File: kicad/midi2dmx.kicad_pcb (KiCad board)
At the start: 4 copper layers, 73.7 x 43.2 mm, 29 parts, among them IC1 MAX485E, P1 MIDI Input, P2 MIDI Through, P3 DMX Out, P4 9V Power, SW1 SW_LED_blue, U1 ProMini

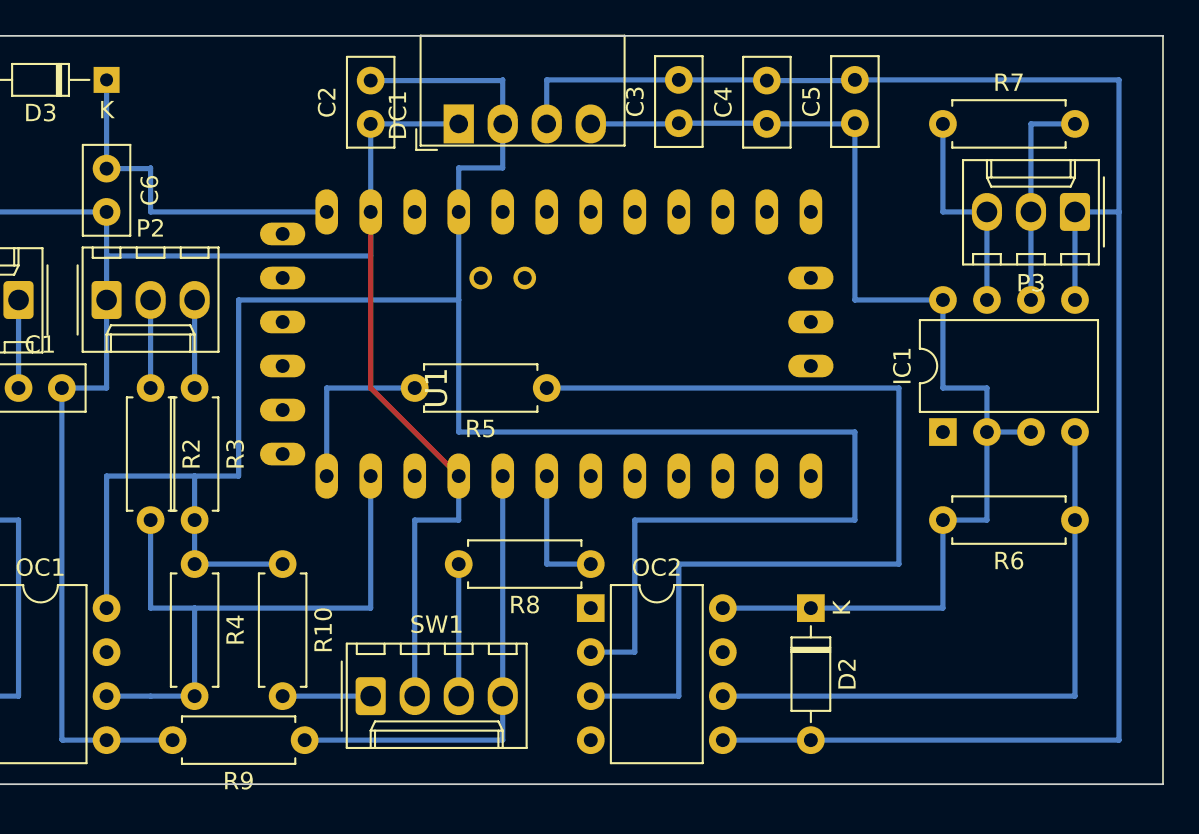
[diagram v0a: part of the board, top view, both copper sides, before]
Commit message: update schematic
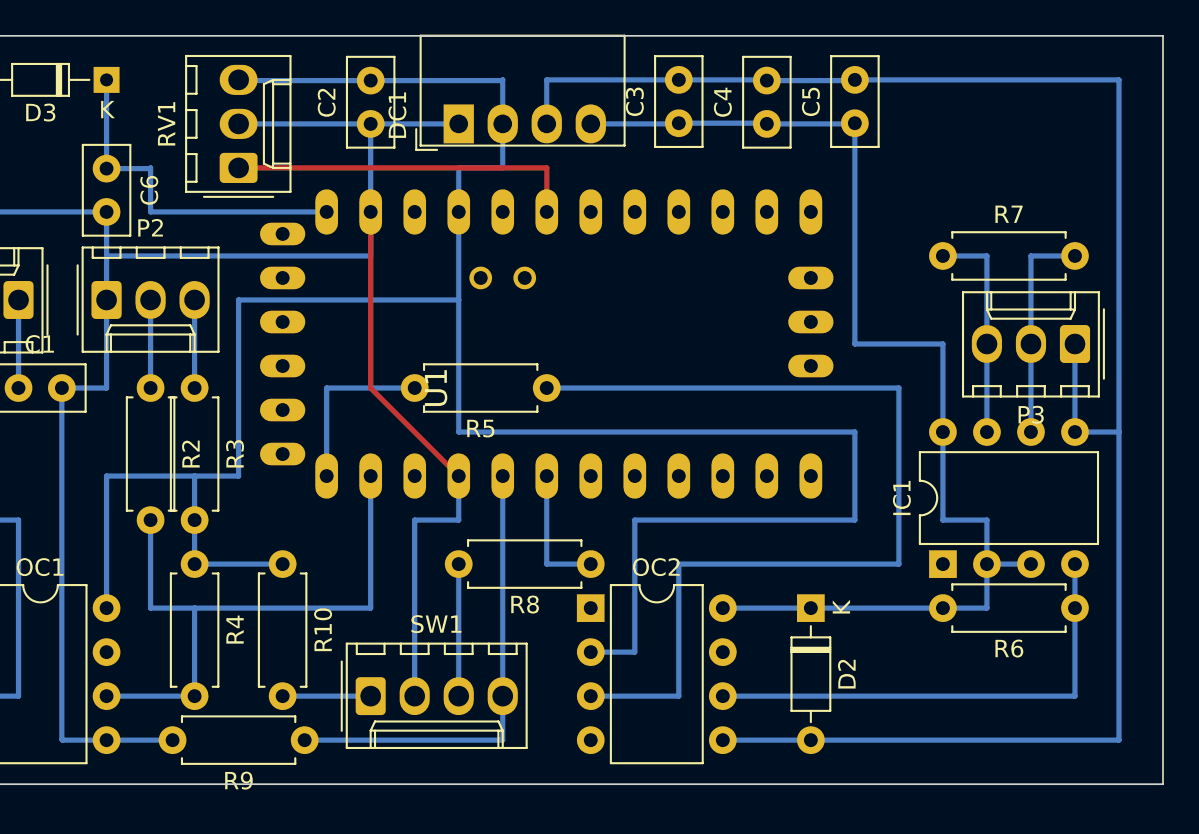
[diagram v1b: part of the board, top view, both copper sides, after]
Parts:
- added RV1: 10k, Connector_Molex:Molex_KK-254_AE-6410-03A_1x03_P2.54mm_Vertical, F.Cu at (83.8, 124.5)
- moved IC1 7.62 mm to (124.5, 147.3)
- moved P3 7.62 mm to (132.1, 134.6)
- moved R7 7.62 mm to (124.5, 129.5)
- moved R6 5.08 mm to (132.1, 149.9)
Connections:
- U1 pad A1: (no net) -> Net-(U1-A1)
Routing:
- net Net-(U1-A1): track 0.00 -> 20.3 mm
- net Net-(IC1-DI): track 35.6 -> 27.9 mm
- net VCC: track 129.6 -> 137.1 mm
- net GND: track 112.7 -> 120.3 mm

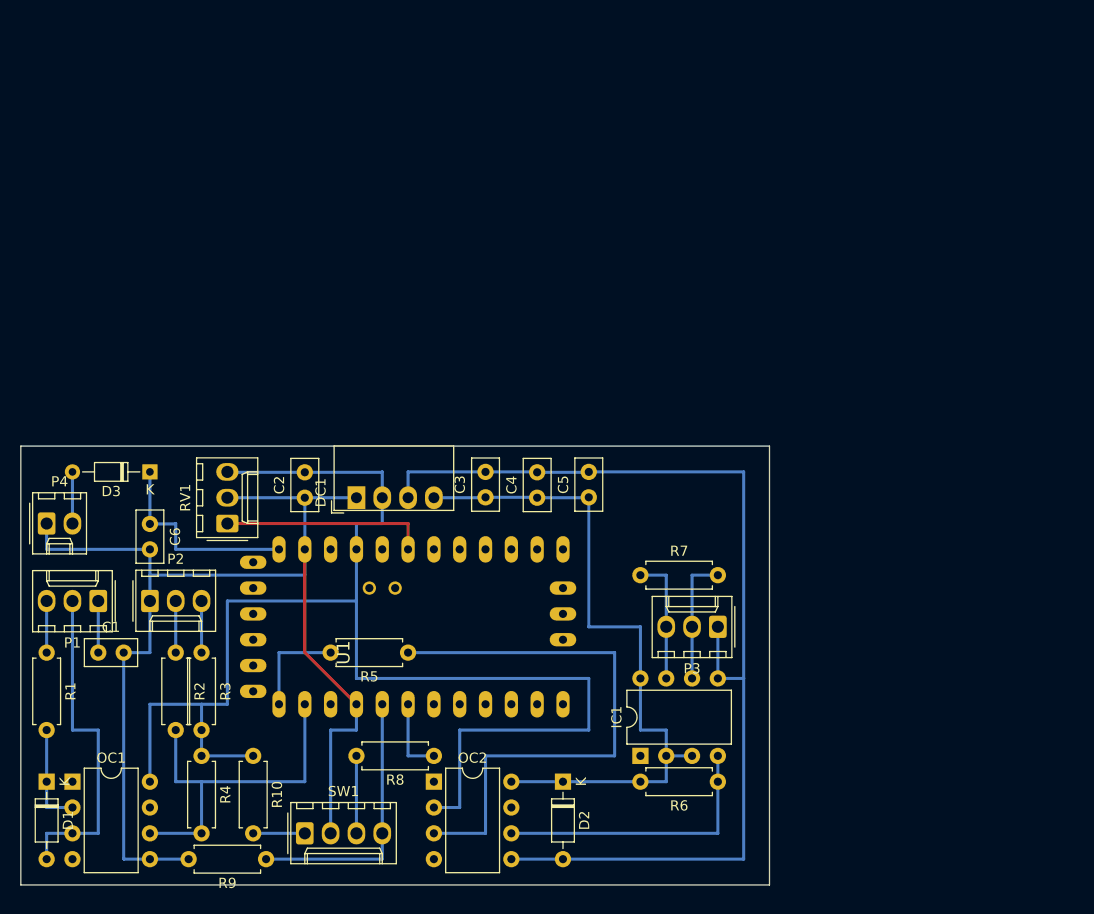
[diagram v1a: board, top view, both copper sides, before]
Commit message: rework PCB to use SMD
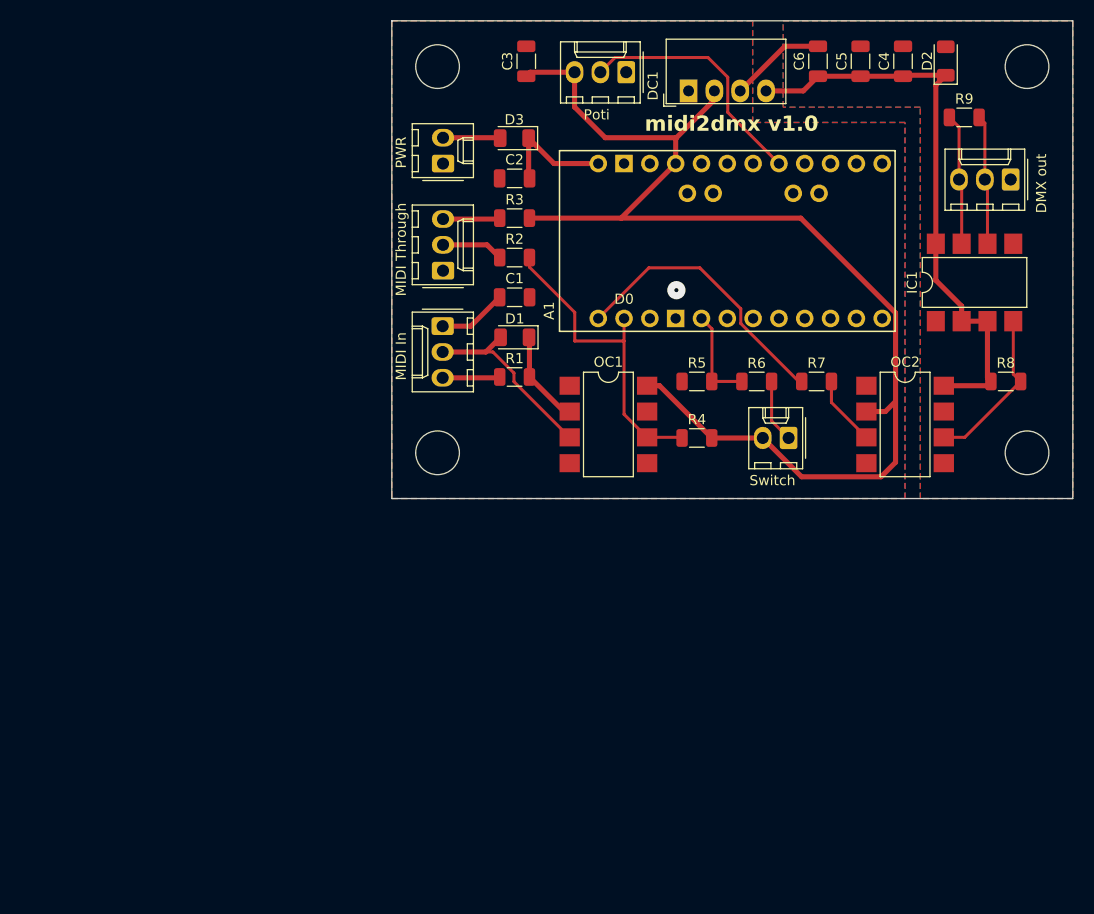
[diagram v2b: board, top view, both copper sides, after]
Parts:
- removed P1: MIDI Input, Connector_Molex:Molex_KK-254_AE-6410-03A_1x03_P2.54mm_Vertical
- removed P2: MIDI Through, Connector_Molex:Molex_KK-254_AE-6410-03A_1x03_P2.54mm_Vertical
- removed P3: DMX Out, Connector_Molex:Molex_KK-254_AE-6410-03A_1x03_P2.54mm_Vertical
- removed P4: 9V Power, Connector_Molex:Molex_KK-254_AE-6410-02A_1x02_P2.54mm_Vertical
- removed R10: 270, Resistor_THT:R_Axial_DIN0207_L6.3mm_D2.5mm_P7.62mm_Horizontal
- removed RV1: 10k, Connector_Molex:Molex_KK-254_AE-6410-03A_1x03_P2.54mm_Vertical
- removed SW1: SW_LED_blue, Connector_Molex:Molex_KK-254_AE-6410-04A_1x04_P2.54mm_Vertical
- removed U1: ProMini, Arduino-clone:ABK-PRO-MINI
- added A1: Arduino_Pro_Mini_Socket_NoSPH, PCM_arduino-library:Arduino_Pro_Mini_Socket_NoSPH, F.Cu at (133.0, 96.7)
- added J1: Conn_01x03, Connector_Molex:Molex_KK-254_AE-6410-03A_1x03_P2.54mm_Vertical, F.Cu at (105.0, 105.0)
- added J2: Conn_01x03, Connector_Molex:Molex_KK-254_AE-6410-03A_1x03_P2.54mm_Vertical, F.Cu at (105.0, 99.6)
- added J3: Conn_01x03, Connector_Molex:Molex_KK-254_AE-6410-03A_1x03_P2.54mm_Vertical, F.Cu at (160.9, 90.6)
- added J4: Conn_01x03, Connector_Molex:Molex_KK-254_AE-6410-03A_1x03_P2.54mm_Vertical, F.Cu at (123.1, 80.1)
- added J5: Conn_01x02, Connector_Molex:Molex_KK-254_AE-6410-02A_1x02_P2.54mm_Vertical, F.Cu at (105.0, 89.0)
- added J6: Conn_01x02, Connector_Molex:Molex_KK-254_AE-6410-02A_1x02_P2.54mm_Vertical, F.Cu at (139.0, 116.0)
- added REF**1: MountingHole_4.3mm_M4, MountingHole:MountingHole_4.3mm_M4, F.Cu at (104.5, 79.5)
- added REF**2: MountingHole_4.3mm_M4, MountingHole:MountingHole_4.3mm_M4, F.Cu at (162.5, 79.5)
- added REF**3: MountingHole_4.3mm_M4, MountingHole:MountingHole_4.3mm_M4, F.Cu at (162.5, 117.5)
- added REF**4: MountingHole_4.3mm_M4, MountingHole:MountingHole_4.3mm_M4, F.Cu at (104.5, 117.5)
- C1, C2, C3, C4, C5, C6: footprint Capacitor_THT:C_Disc_D5.0mm_W2.5mm_P2.50mm -> Capacitor_SMD:C_1206_3216Metric
- D1, D2: footprint Diode_THT:D_DO-35_SOD27_P7.62mm_Horizontal -> Diode_SMD:D_1206_3216Metric
- D3: footprint Diode_THT:D_DO-34_SOD68_P7.62mm_Horizontal -> Diode_SMD:D_1206_3216Metric
- IC1, OC1, OC2: footprint Package_DIP:DIP-8_W7.62mm -> Package_DIP:SMDIP-8_W7.62mm
- R1, R2, R3, R4: footprint Resistor_THT:R_Axial_DIN0207_L6.3mm_D2.5mm_P7.62mm_Horizontal -> Resistor_SMD:R_1206_3216Metric
- R5: value 470 -> 100k; footprint Resistor_THT:R_Axial_DIN0207_L6.3mm_D2.5mm_P7.62mm_Horizontal -> Resistor_SMD:R_1206_3216Metric
- R6: value 4.7k -> 270; footprint Resistor_THT:R_Axial_DIN0207_L6.3mm_D2.5mm_P7.62mm_Horizontal -> Resistor_SMD:R_1206_3216Metric
- R7: value 120 -> 470; footprint Resistor_THT:R_Axial_DIN0207_L6.3mm_D2.5mm_P7.62mm_Horizontal -> Resistor_SMD:R_1206_3216Metric
- R8: value 91 -> 4.7k; footprint Resistor_THT:R_Axial_DIN0207_L6.3mm_D2.5mm_P7.62mm_Horizontal -> Resistor_SMD:R_1206_3216Metric
- R9: value 100K -> 120; footprint Resistor_THT:R_Axial_DIN0207_L6.3mm_D2.5mm_P7.62mm_Horizontal -> Resistor_SMD:R_1206_3216Metric
- moved R9 100.2 mm to (156.3, 84.5), turned to 0 degrees
- moved D2 80.3 mm to (154.5, 79.0), turned to 90 degrees
- moved C6 80.0 mm to (141.9, 79.0), turned to 90 degrees
- moved R8 67.3 mm to (160.4, 110.5), turned to 0 degrees
- moved D1 63.5 mm to (112.1, 106.1), turned to 180 degrees
- moved OC1 63.4 mm to (121.3, 114.7)
- moved OC2 58.2 mm to (150.5, 114.7)
- moved R4 57.9 mm to (130.0, 116.0), turned to 180 degrees
- moved IC1 57.0 mm to (157.3, 100.7)
- moved C4 56.0 mm to (150.3, 79.0)
- moved C1 53.9 mm to (112.1, 102.2)
- moved R1 53.4 mm to (112.1, 110.0), turned to 0 degrees
- moved R3 52.7 mm to (112.1, 94.4), turned to 0 degrees
- moved DC1 51.7 mm to (129.2, 81.9)
- moved R2 51.2 mm to (112.1, 98.3), turned to 0 degrees
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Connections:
- net Net-(D1-A) renamed /MIDI IN Pin5 SIG
- net Net-(OC1-VO) renamed D0/RX
- C1 pad 1: Net-(C1-Pad1) -> /MIDI IN Pin2 GND
- C2 pad 1: GND -> +9V
- C2 pad 2: VCC -> GND
- C3 pad 1: +5V -> GND
- C3 pad 2: GND2 -> VCC
- C6 pad 1: Net-(D3-K) -> +5V
- C6 pad 2: GND -> GND2
- D3 pad 1: Net-(D3-K) -> +9V
- D3 pad 2: Net-(D3-A) -> /PWR 9V+
- IC1 pad 6: Net-(IC1-A) -> /DMX OUT Pin2 -
- IC1 pad 7: Net-(IC1-B) -> /DMX OUT Pin3 +
- OC1 pad 4: (no net) -> unconnected-(OC1-NC-Pad4)
- OC2 pad 4: (no net) -> unconnected-(OC2-NC-Pad4)
- R1 pad 1: Net-(P1-Pad4) -> /MIDI IN Pin4 5V+
- R2 pad 1: Net-(P2-Pad5) -> /MIDI THROUGH Pin5 SIG
- R3 pad 1: Net-(P2-Pad4) -> /MIDI THROUGH Pin4 5V+
- R5 pad 1: Net-(OC2-C) -> GND
- R5 pad 2: Net-(U1-TX0_D1) -> D2
- R6 pad 1: Net-(IC1-DI) -> /SW 5V+
- R6 pad 2: +5V -> D2
- R7 pad 1: Net-(IC1-B) -> D1/TX
- R7 pad 2: Net-(IC1-A) -> Net-(OC2-C)
- R8 pad 1: Net-(U1-D3) -> +5V
- R8 pad 2: Net-(SW1-K) -> Net-(IC1-DI)
- R9 pad 1: Net-(SW1-A) -> /DMX OUT Pin3 +
- R9 pad 2: GND -> /DMX OUT Pin2 -
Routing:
- net GND: track 120.3 -> 0.00 mm, vias 0 -> 1
- net GND2: track 104.1 -> 9.47 mm
- net Net-(OC2-C): track 55.9 -> 6.92 mm
- net D1/TX: track 0.00 -> 27.6 mm
- net Net-(SW1-A): track 26.7 -> 0.00 mm
- net /POTI Pin2: track 0.00 -> 24.5 mm
- net Net-(D3-K): track 20.4 -> 0.00 mm
- net Net-(U1-A1): track 20.3 -> 0.00 mm
- net /MIDI IN Pin5 SIG: track 33.0 -> 18.5 mm
- net VCC: track 137.1 -> 122.6 mm
- net /DMX OUT Pin3 +: track 0.00 -> 12.9 mm
- net /DMX OUT Pin2 -: track 0.00 -> 12.8 mm
- net Net-(IC1-A): track 12.7 -> 0.00 mm
- net Net-(IC1-B): track 12.7 -> 0.00 mm
- net +9V: track 0.00 -> 11.9 mm
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- added copper zone on B.Cu, net GND
- added copper zone on F.Cu, net GND
- added copper zone on B.Cu, net GND2
- added copper zone on F.Cu, net GND2
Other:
- board size 73.7 x 43.2 mm -> 67 x 47 mm
- copper layers 4 -> 2
- board text added: "DMX out"
- board text added: "MIDI In"
- board text added: "MIDI Through"
- board text added: "PWR"
- board text added: "Poti"
- board text added: "Switch"
- board text added: "midi2dmx v1.0"
